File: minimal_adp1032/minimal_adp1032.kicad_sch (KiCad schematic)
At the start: 46 parts, among them T1 ZA9644-AED, U1 ADP1032ACPZ-5-R7

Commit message: minor updates
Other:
- moved on the sheet: C1, C2, C3, C4, C5, C6, C7, D1, D2, D3, JP1, JP2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

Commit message: minor updates
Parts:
- U1: MPN (none) -> ADP1032ACPZ-5-R7
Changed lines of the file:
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@@
+			)
+		)
+		(property "MPN" "ADP1032ACPZ-5-R7"
+			(at 162.56 162.56 0)
+			(effects
+				(font
+					(size 1.27 1.27)
+				)
+				(justify left)
+				(hide yes)
 			)
 		)

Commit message: Minor updates
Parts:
- added J1, J2: FW-07-03-G-D-085-155, connector_footprints:FW-07-03-G-D-085-155, symbol UNITED_CONNECTORS_DATA_BASE:J_FW-07-03-G-D-085-155
- added J3, J4, J5, J6: FW-02-03-G-D-085-155, connector_footprints:FW-02-03-G-D-085-155, symbol UNITED_CONNECTORS_DATA_BASE:J_FW-02-03-G-D-085-155
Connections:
- net GND: now also J3.2, J3.4
- net GNDA: now also J2.1, J2.11, J2.13, J2.3, J2.5, J2.7, J2.9, J4.2, J4.4, J6.1, J6.3
- net GNDD: now also J1.10, J1.12, J1.14, J1.2, J1.4, J1.6, J1.8, J5.2, J5.4
- net MCK: now also J1.7
- net MGPI1: now also J1.1
- net MGPI2: now also J1.3
- net MGPO3: now also J1.5
- net MI: now also J1.11
- net MO: now also J1.9
- net MVDD: now also J5.1, J5.3
- net SCK: now also J2.8
- net SGPI3: now also J2.6
- net SI: now also J2.10
- net SO: now also J2.12
- net SPGO1: now also J2.2
- net SPGO2: now also J2.4
- net VDD_24V: now also J4.1, J4.3
- net VINP: now also J3.1, J3.3
- net ~{MSS}: now also J1.13
- net ~{SSS}: now also J2.14
- net 3V3_ISO renamed 3V3
- net 3V3: now also J6.2, J6.4
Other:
- moved on the sheet: TP1, TP10, TP11, TP12, TP13, TP14, TP2, TP3, TP4, TP5, TP6, TP7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

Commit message: Minor updates
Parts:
- added TP13, TP5: TestPoint, test_point_footprints:TestPoint_THTPad_Castelated, symbol UNITED_TEST_POINTS:TestPoint_Castelated
- J3: renamed from J1; footprint connector_footprints:FW-07-03-G-D-085-155 -> connector_footprints:FW-08-03-G-D-085-155; symbol UNITED_CONNECTORS_DATA_BASE:J_FW-07-03-G-D-085-155 -> UNITED_CONNECTORS_DATA_BASE:J_FW-08-03-G-D-085-155; MPN FW-07-03-G-D-085-155 -> FW-08-03-G-D-085-155; Pin Count 7 -> 8; Symbol Name J_FW-07-03-G-D-085-155 -> J_FW-08-03-G-D-085-155; Trustedparts Search https://www.trustedparts.com/en/search/FW-07-03-G-D-085-155 -> https://www.trustedparts.com/en/search/FW-08-03-G-D-085-155
- J4: renamed from J2; footprint connector_footprints:FW-07-03-G-D-085-155 -> connector_footprints:FW-08-03-G-D-085-155; symbol UNITED_CONNECTORS_DATA_BASE:J_FW-07-03-G-D-085-155 -> UNITED_CONNECTORS_DATA_BASE:J_FW-08-03-G-D-085-155; MPN FW-07-03-G-D-085-155 -> FW-08-03-G-D-085-155; Pin Count 7 -> 8; Symbol Name J_FW-07-03-G-D-085-155 -> J_FW-08-03-G-D-085-155; Trustedparts Search https://www.trustedparts.com/en/search/FW-07-03-G-D-085-155 -> https://www.trustedparts.com/en/search/FW-08-03-G-D-085-155
- renumbered C5 to C1, C1 to C2, C2 to C5, D2 to D1, D3 to D2, D1 to D3, J5 to J1, J3 to J2, J6 to J5, J4 to J6, JP3 to JP1, JP1 to JP2, JP2 to JP3, R8 to R1, R4 to R3, R6 to R4, R3 to R6, R1 to R7, R7 to R8, TP18 to TP1, TP14 to TP10, TP13 to TP11, TP7 to TP14, TP6 to TP15, TP5 to TP16, TP4 to TP17, TP1 to TP18, TP2 to TP19, TP22 to TP2, TP3 to TP20, TP15 to TP21, TP19 to TP22, TP27 to TP24, TP26 to TP3, TP30 to TP4, TP8 to TP6, TP9 to TP7, TP10 to TP8, TP11 to TP9
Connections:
- net GNDA: now also J4.10, J4.12, J4.14, J4.16, J4.2, J4.4, J4.6, J4.8, TP13.1; no longer J4.11, J4.13, J4.3, J4.5, J4.7, J4.9
- net GNDD: now also J3.1, J3.11, J3.13, J3.15, J3.3, J3.5, J3.7, J3.9, TP5.1; no longer J3.10, J3.12, J3.14, J3.4, J3.6, J3.8
- net MCK: now also J3.10; no longer J3.7
- net MGPI1: now also J3.16; no longer J3.1
- net MGPI2: now also J3.14; no longer J3.3
- net MGPO3: now also J3.12; no longer J3.5
- net MI: now also J3.6; no longer J3.11
- net MO: now also J3.8; no longer J3.9
- net SCK: now also J4.9; no longer J4.8
- net SGPI3: now also J4.11; no longer J4.6
- net SI: now also J4.7; no longer J4.10
- net SO: now also J4.5; no longer J4.12
- net SPGO1: now also J4.15; no longer J4.2
- net SPGO2: now also J4.13; no longer J4.4
- net ~{MSS}: now also J3.4; no longer J3.13
- net ~{SSS}: now also J4.3; no longer J4.14

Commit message: Backup
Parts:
- C1: footprint capacitor_footprints:C_1210_3225Metric -> capacitor_footprints:C_1210_200_3225Metric; 3dviewer Link (none) -> https://3dviewer.net/index.html#model=https://github.com/io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; Capacitor Type (none) -> Ceramic; Case Code - in 1210 -> 1210_200; Series GCM32D -> GCM32DC72A
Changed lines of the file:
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@@
 			)
 		)
-		(property "Footprint" "capacitor_footprints:C_1210_3225Metric"
+		(property "Footprint" "capacitor_footprints:C_1210_200_3225Metric"
 			(at 99.06 41.91 0)
 			(show_name yes)
@@
 			)
 		)
-		(property "Description" "CAP SMD 4.7 µF X7S 10% 1210 100V"
+		(property "Description" "CAP SMD 4.7 µF X7S 10% 1210_200 100V"
 			(at 93.98 41.91 0)
 			(show_name yes)
@@
 			)
 		)
-		(property "Case Code - in" "1210"
+		(property "Case Code - in" "1210_200"
 			(at 91.44 41.91 0)
 			(show_name yes)
@@
 			)
 		)
-		(property "Series" "GCM32D"
+		(property "Series" "GCM32DC72A"
 			(at 78.74 41.91 0)
 			(show_name yes)
@@
 				(hide yes)
 			)
+		)
+		(property "3dviewer Link" "https://3dviewer.net/index.html#model=https://github.com/ionutms/KiCAD_Symbols_Generator/blob/main/3D_models/C_1210.step"
+			(at 91.44 41.91 0)
+			(effects
+				(font
+					(size 1.27 1.27)
+				)
+				(justify left)
+				(hide yes)
+			)
+		)
+		(property "Capacitor Type" "Ceramic"
+			(at 88.9 41.91 0)
+			(effects
+				(font
+					(size 1.27 1.27)
+				)
+				(justify left)
+				(hide yes)
+			)

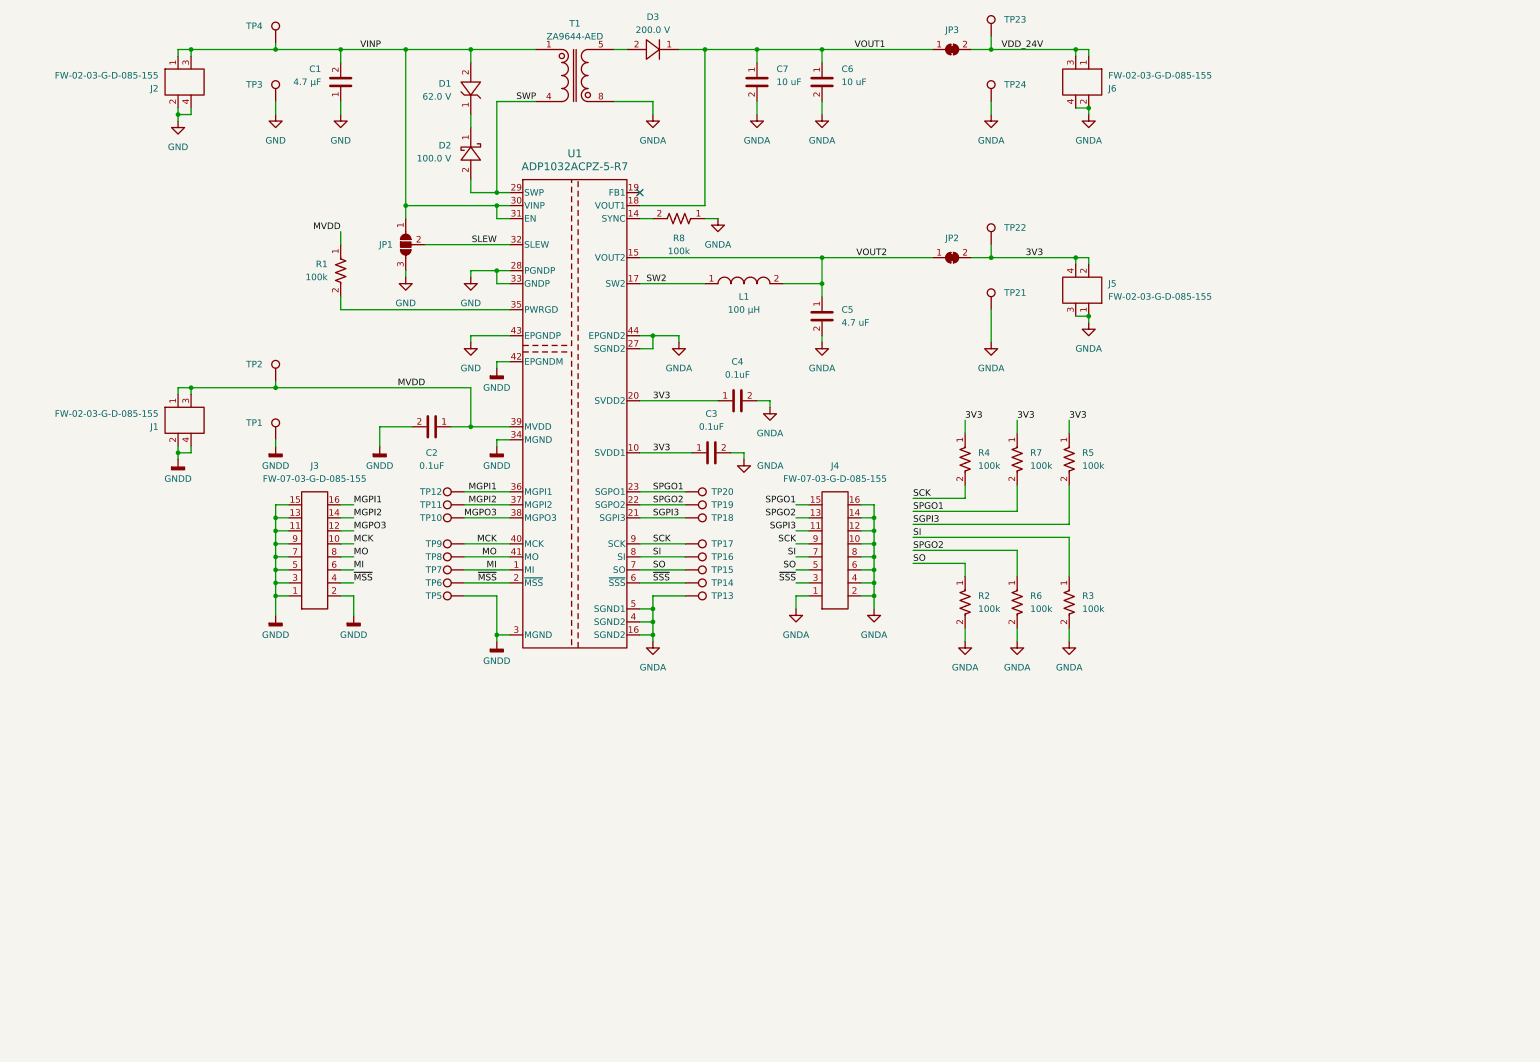
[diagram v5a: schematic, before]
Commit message: Update KiCAD Symbol Generator subproject and enhance component libraries
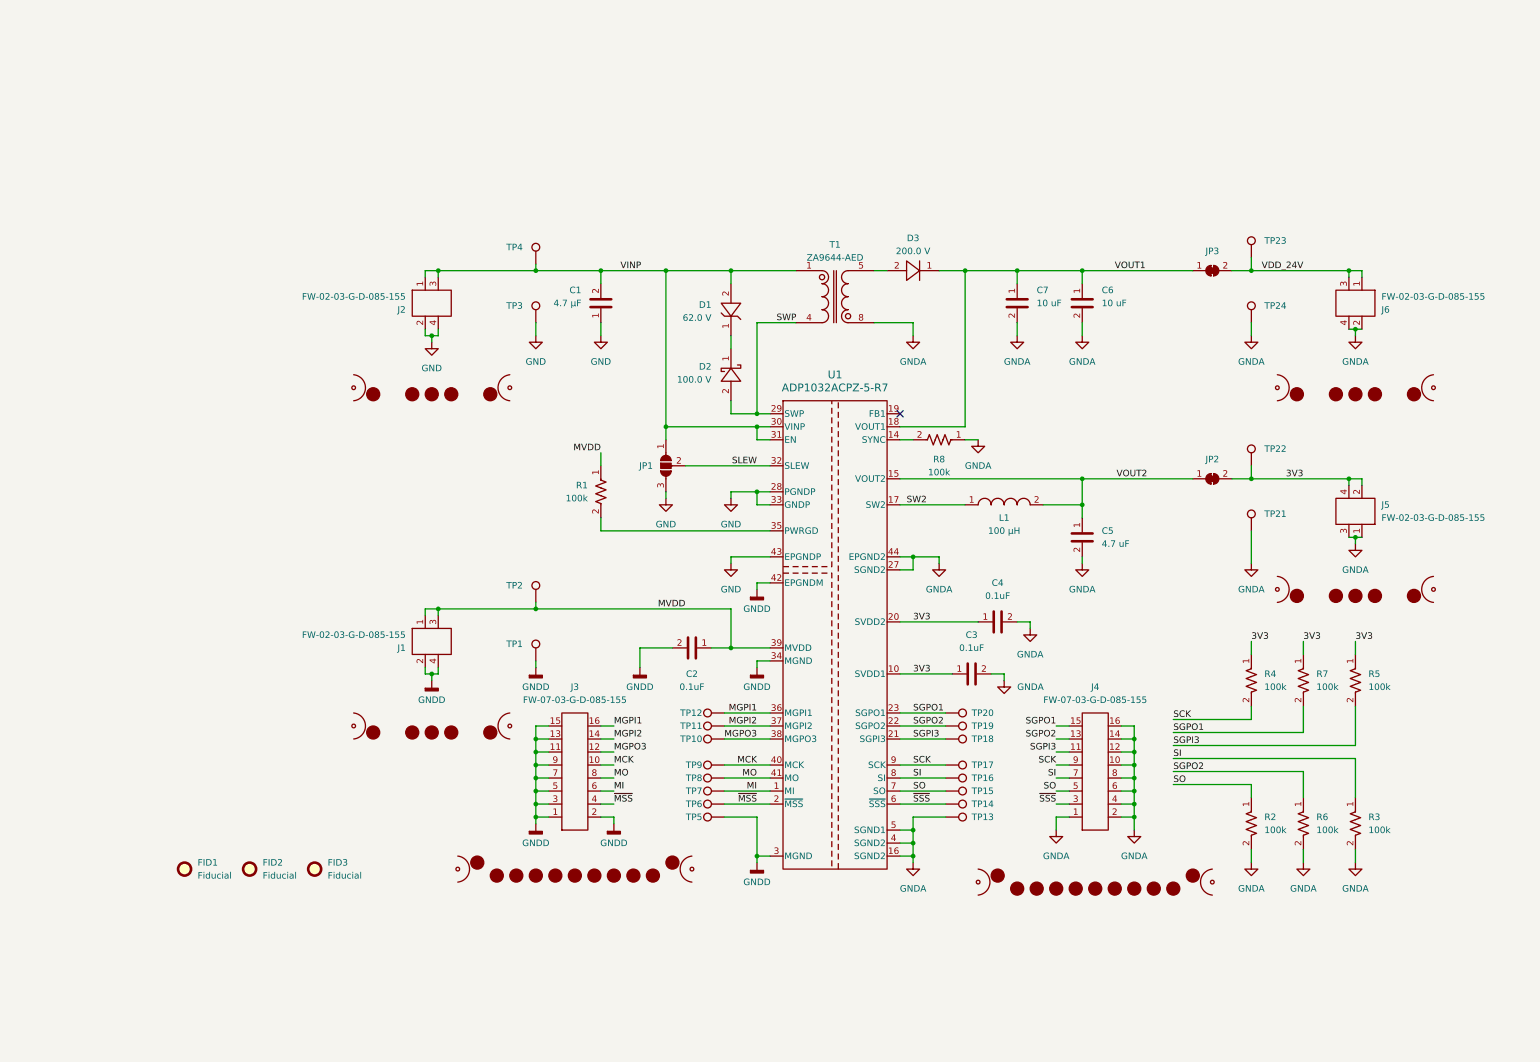
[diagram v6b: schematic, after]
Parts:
- added FID1, FID2, FID3: Fiducial, no_components_footprints:Fiducial_0.5mm_Mask1mm, symbol UNITED_NO_COMPONENTS_DATA_BASE:Fiducial
- added MB1, MB2, MB3, MB4: mouse-bite-midle-50mil-200mil, mouse_bite_footprints:mouse-bite-50mil-305mil, symbol UNITED_MOUSE_BITES_DATA_BASE:mouse-bite-50mil-305mil
- added MB5, MB6: mouse-bite-midle-50mil-200mil, mouse_bite_footprints:mouse-bite-50mil-500mil, symbol UNITED_MOUSE_BITES_DATA_BASE:mouse-bite-50mil-500mil
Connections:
- net SPGO1 renamed SGPO1
- net SPGO2 renamed SGPO2
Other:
- moved on the sheet: C1, C2, C3, C4, C5, C6, C7, D1, D2, D3, J1, J2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

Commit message: Switch to KiCad 9
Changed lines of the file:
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@@
 (kicad_sch
-	(version 20231120)
+	(version 20250114)
 	(generator "eeschema")
-	(generator_version "8.0")
+	(generator_version "9.0")
 	(paper "A3")
 	(junction
@@
 		)
 	)
+	(embedded_fonts no)
 )

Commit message: Add new images and update project configuration for minimal_adp1032
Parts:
- C2, C3, C4: value 0.1uF -> 100 nF; 3dviewer Link (none) -> https://3dviewer.net/index.html#model=https://github.com/io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; Capacitor Type (none) -> Ceramic; Series GCM155 -> GCM155R71H
- C5: value 4.7 uF -> 4.7 µF; 3dviewer Link (none) -> https://3dviewer.net/index.html#model=https://github.com/io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; Capacitor Type (none) -> Ceramic
- C6, C7: value 10 uF -> 10 µF; 3dviewer Link (none) -> https://3dviewer.net/index.html#model=https://github.com/io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; Capacitor Type (none) -> Ceramic; Series CL31 -> CL31B
- J3, J4: value FW-07-03-G-D-085-155 -> FW-08-03-G-D-085-155
- R1, R2, R3, R4, R5, R6, R7, R8: value 100k -> 100 kΩ; 3dviewer Link (none) -> https://3dviewer.net/index.html#model=https://github.com/io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; Component Type (none) -> Resistor; Series ERJ-2GE -> ERJ-2GEJ; Temperature Coefficient (none) -> 200 ppm/°C
- T1: 3dviewer Link (none) -> https://3dviewer.net/index.html#model=https://github.com/io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; Maximum DC Resistance (Ω) 1.800 -> pri = 1.8; sec = 1.8; Primary Inductance (µH) (none) -> 470; Turns Ratio (none) -> pri : sec = 1 : 1
